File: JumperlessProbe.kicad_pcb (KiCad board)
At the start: 2 copper layers, 123.2 x 25.4 mm, 18 parts, among them J1 Conn_01x02, J2 Conn_01x01, J3 Conn_01x01, J4 Conn_01x01, SW1 SW_DIP_x01

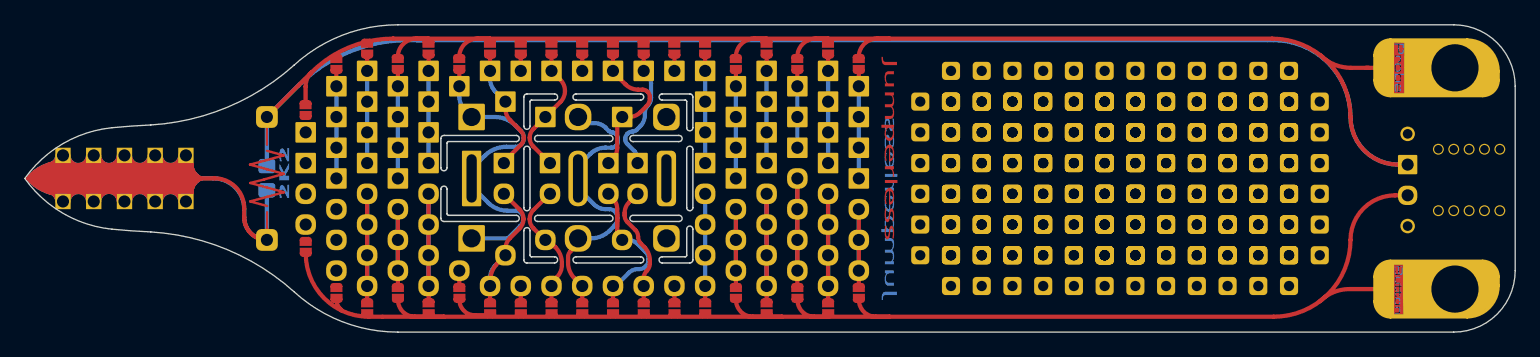
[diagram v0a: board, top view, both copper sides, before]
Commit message: Widened NPTHs
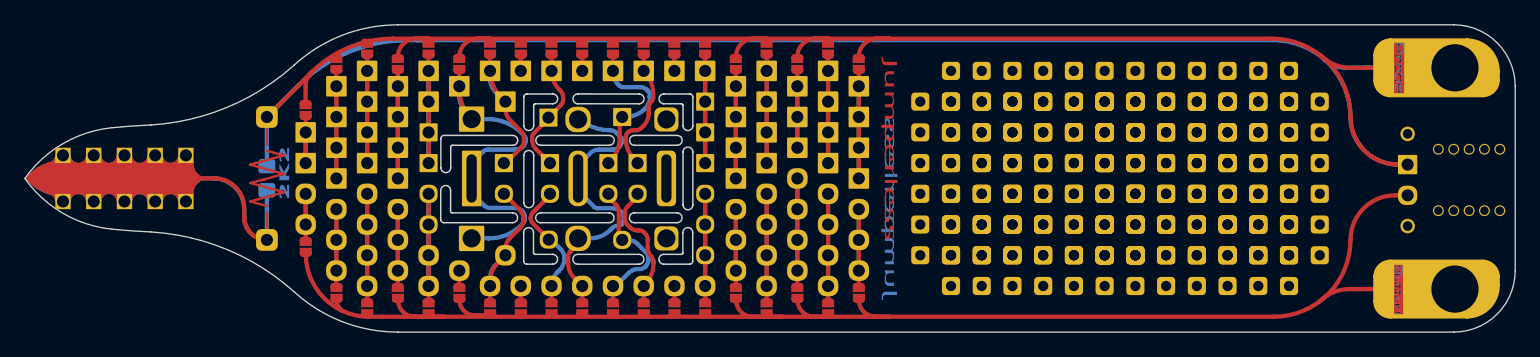
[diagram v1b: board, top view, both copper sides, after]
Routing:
- net Net-(J1-Pin_1): track 393.2 -> 489.7 mm
- net Net-(J1-Pin_2): track 325.5 -> 356.0 mm

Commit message: see if gitignore works
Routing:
- net Net-(J1-Pin_1): track 489.7 -> 488.4 mm
- net Net-(J1-Pin_2): track 356.0 -> 354.8 mm
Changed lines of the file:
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@@
-	)
-	(arc
-		(start 61.468 45.212494)
-		(mid 62.030686 45.588469)
-		(end 62.69442 45.720494)
-		(width 0.35)
-		(layer "B.Cu")
-		(net 1)
 	)
 	(arc
@@
 	)
 	(segment
-		(start 70.776 55.959994)
-		(end 70.776 56.166494)
-		(width 0.35)
-		(layer "F.Cu")
-		(net 2)
-	)
-	(segment
 		(start 65.940437 54.935055)
 		(end 65.139463 55.73603)
@@
 	)
 	(arc
-		(start 70.776 55.959994)
-		(mid 70.723197 55.880969)
-		(end 70.629982 55.899511)
-		(width 0.35)
-		(layer "F.Cu")
-		(net 2)
-	)
-	(arc
 		(start 95.383806 62.23)
 		(mid 94.396327 61.820973)
@@
 	)
 	(segment
-		(start 70.776 45.923694)
-		(end 70.662901 45.807499)
-		(width 0.35)
-		(layer "B.Cu")
-		(net 2)
-	)
-	(segment
 		(start 69.215 56.515)
 		(end 69.341471 56.641471)
@@
 	)
 	(segment
-		(start 70.460722 45.553973)
-		(end 70.288201 45.279404)
-		(width 0.35)
-		(layer "B.Cu")
-		(net 2)
-	)
-	(segment
 		(start 75.7138 58.293494)
 		(end 75.82231 58.293494)
@@
 		(width 0.35)
 		(layer "B.Cu")
-		(net 2)
-	)
-	(segment
-		(start 70.662901 45.807499)
-		(end 70.460722 45.553973)
-		(width 0.35)
-		(layer "B.Cu")
